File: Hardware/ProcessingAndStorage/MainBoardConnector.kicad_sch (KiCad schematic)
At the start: 1 part

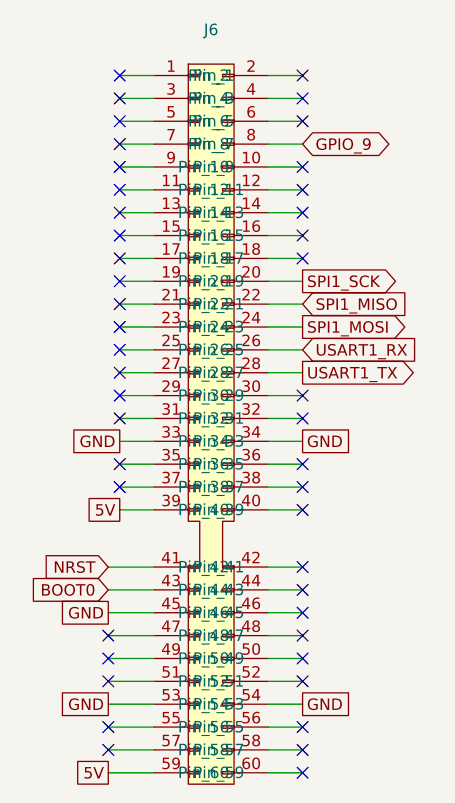
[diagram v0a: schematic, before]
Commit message: rework CI, make PCB smaller
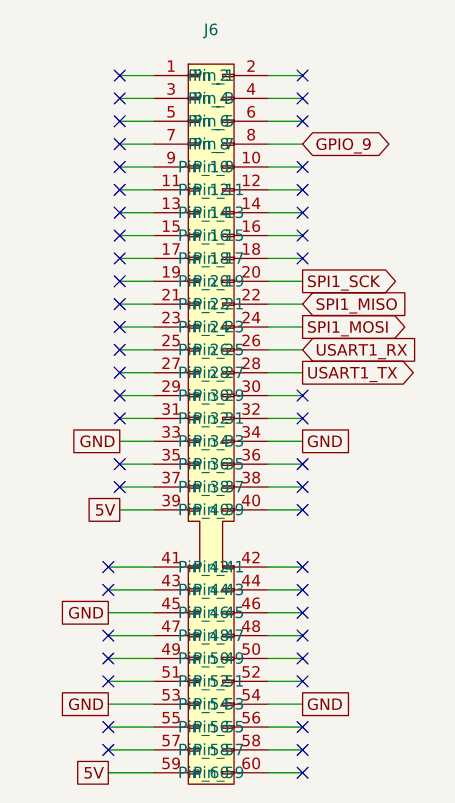
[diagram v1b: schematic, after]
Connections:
- net BOOT0: no longer names the net of J6.43 (Pin_43)
- net NRST: no longer names the net of J6.41 (Pin_41)
- no-connect marks 45 -> 47
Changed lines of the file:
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@@
+	)
+	(no_connect
+		(at 59.69 90.17)
 	)
 	(no_connect
 		(at 81.28 71.12)
+	)
+	(no_connect
+		(at 59.69 87.63)
 	)
 	(no_connect
@@
 		)
 	)
-	(global_label "NRST"
-		(shape input)
-		(at 59.69 87.63 180)
-		(fields_autoplaced yes)
-		(effects
-			(font
-				(size 1.27 1.27)
-			)
-			(justify right)
-		)
-		(property "Intersheetrefs" "${INTERSHEET_REFS}"
-			(at 51.9272 87.63 0)
-			(effects
-				(font
-					(size 1.27 1.27)
-				)
-				(justify right)
-				(hide yes)
-			)
-		)
-	)
 	(global_label "USART1_RX"
 		(shape input)
@@
 				(hide yes)
 			)
-		)
-	)
-	(global_label "BOOT0"
-		(shape input)
-		(at 59.69 90.17 180)
-		(fields_autoplaced yes)
-		(effects
-			(font
-				(size 1.27 1.27)
-			)
-			(justify right)
-		)
-		(property "Intersheetrefs" "${INTERSHEET_REFS}"
-			(at 50.5967 90.17 0)
-			(effects
-				(font
-					(size 1.27 1.27)
-				)
-				(justify right)
-				(hide yes)
-			)
